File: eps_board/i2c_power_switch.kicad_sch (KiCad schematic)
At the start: 6 parts, among them U25 MCP23008T-E/SS

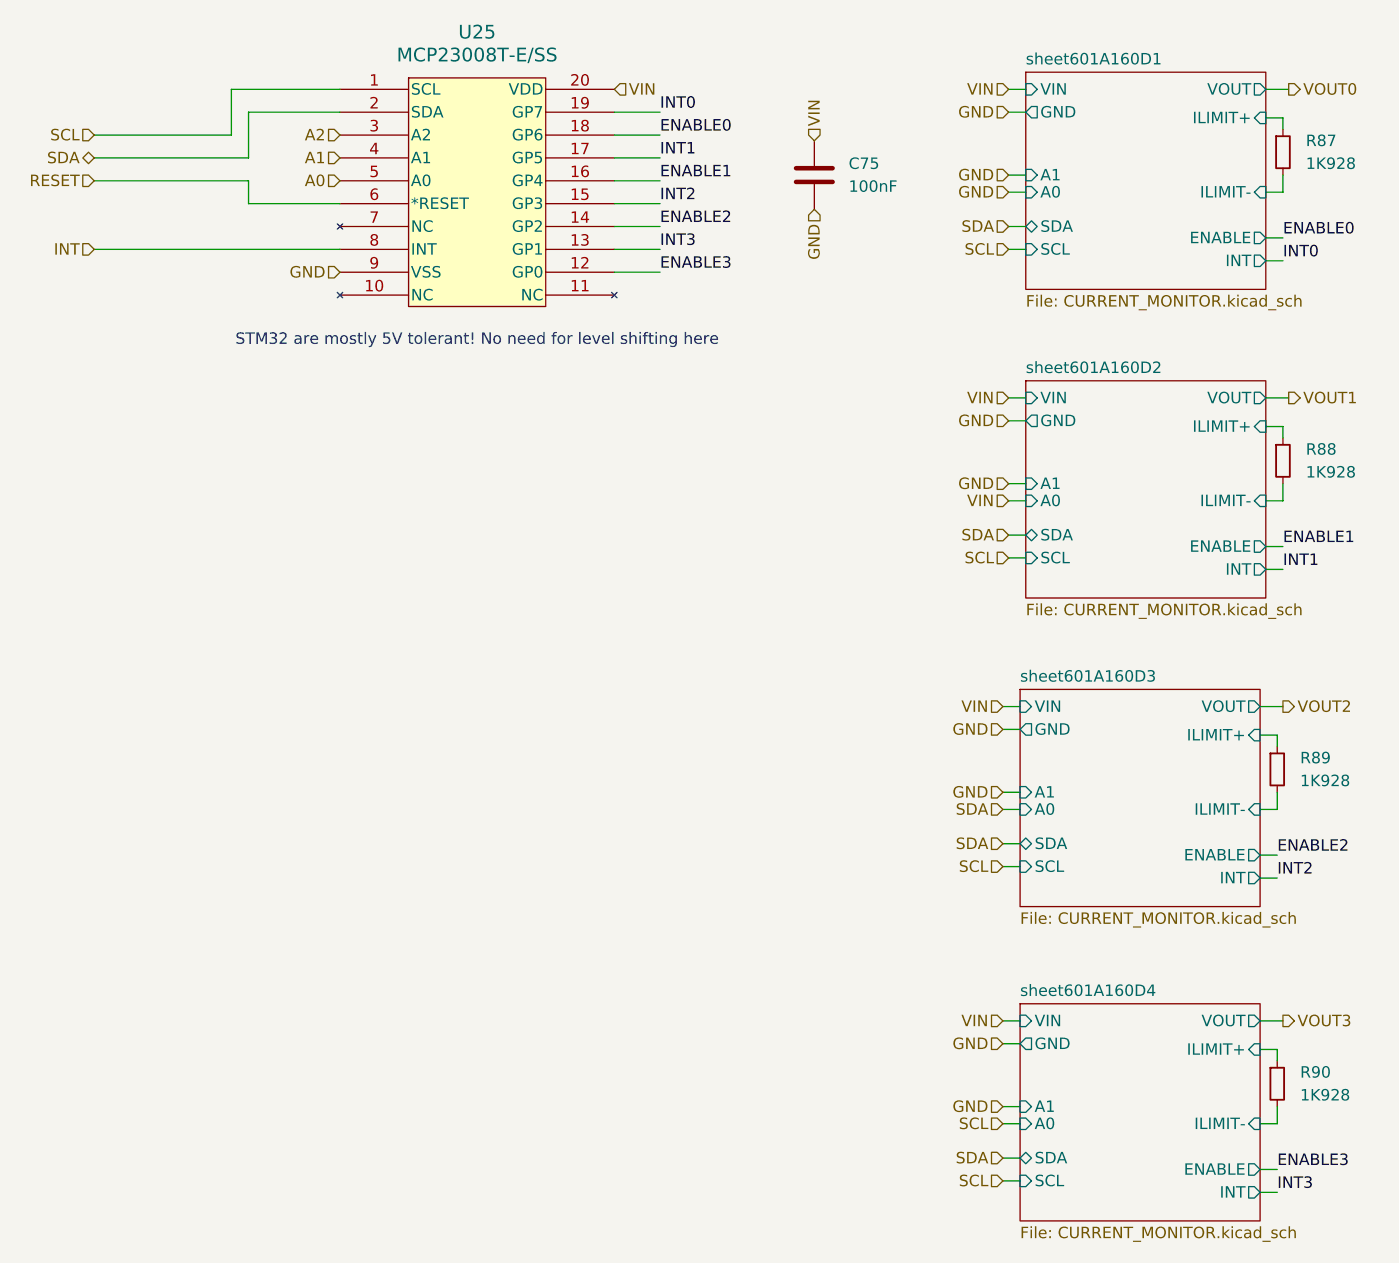
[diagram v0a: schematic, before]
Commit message: cleaning up bom: remove main camera port since it has not pullups and capacitors, correcting some errors in camera switch
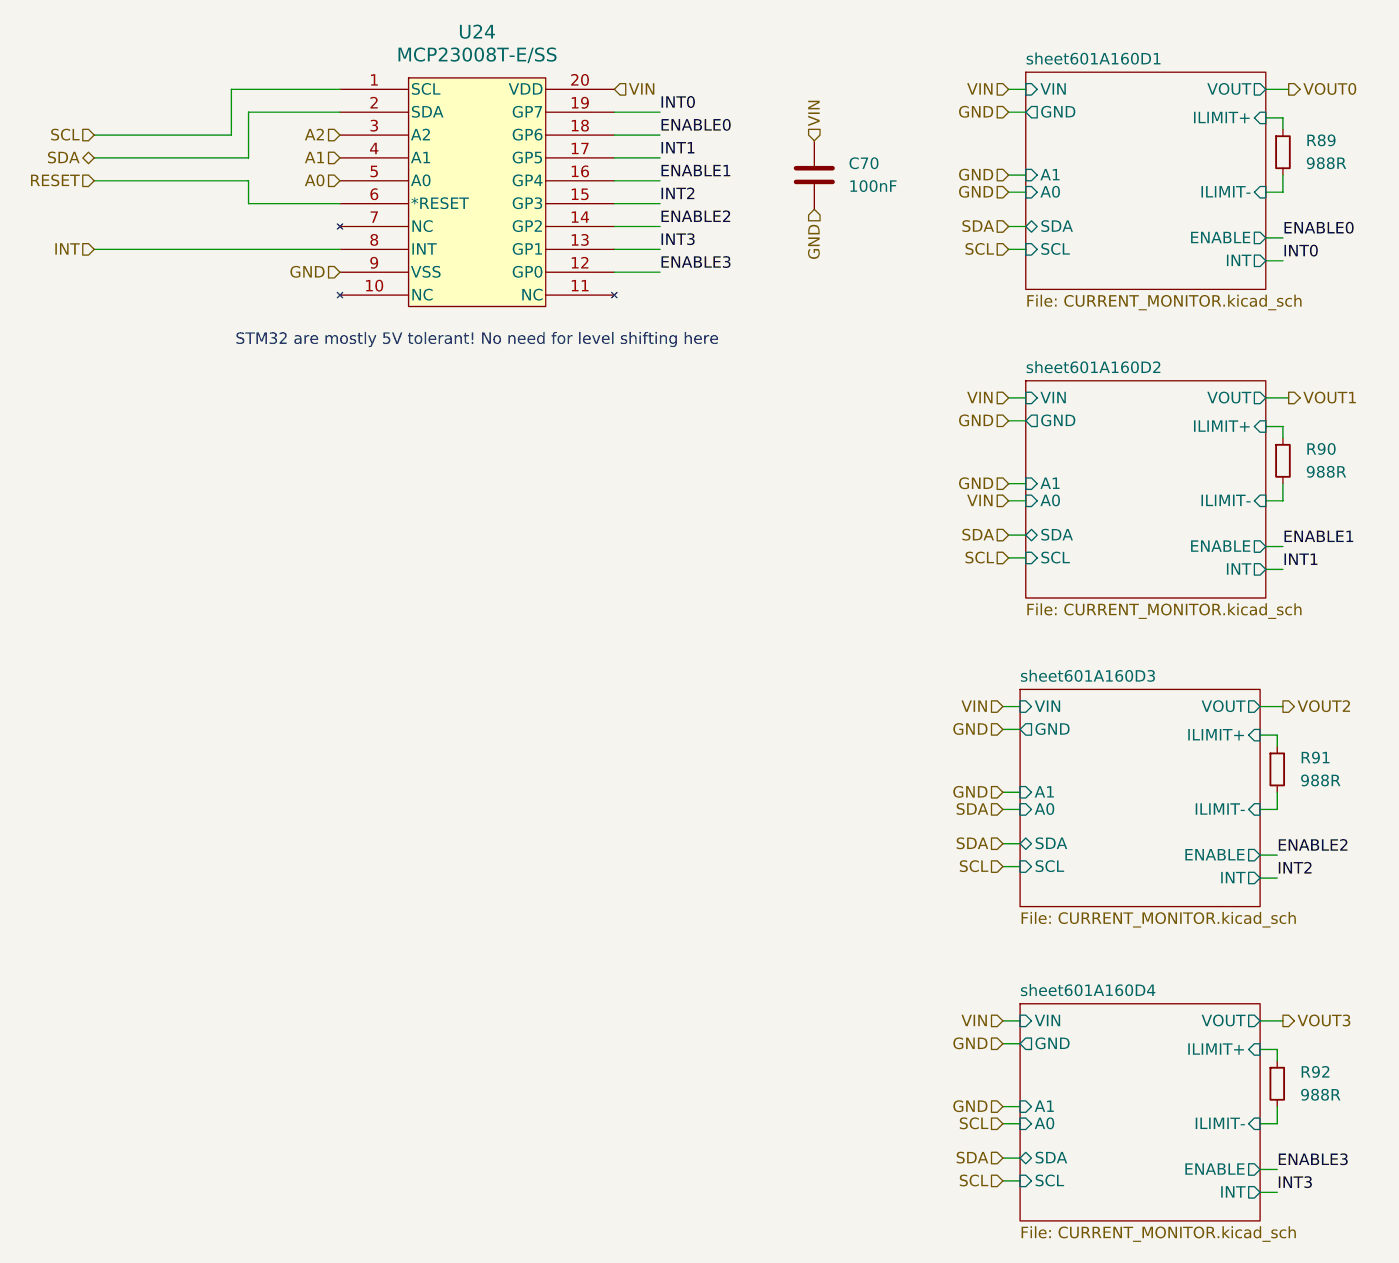
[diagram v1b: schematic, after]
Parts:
- R89: renamed from R87; value 1K928 -> 988R; Part Number RC0603FR-071K928L -> RT0603DRE07988RL; Tolerance 1 -> 0.5
- R90: renamed from R88; value 1K928 -> 988R; Part Number RC0603FR-071K928L -> RT0603DRE07988RL; Tolerance 1 -> 0.5
- R91: renamed from R89; value 1K928 -> 988R; Part Number RC0603FR-071K928L -> RT0603DRE07988RL; Tolerance 1 -> 0.5
- R92: renamed from R90; value 1K928 -> 988R; Part Number RC0603FR-071K928L -> RT0603DRE07988RL; Tolerance 1 -> 0.5
- renumbered C75 to C70, U25 to U24

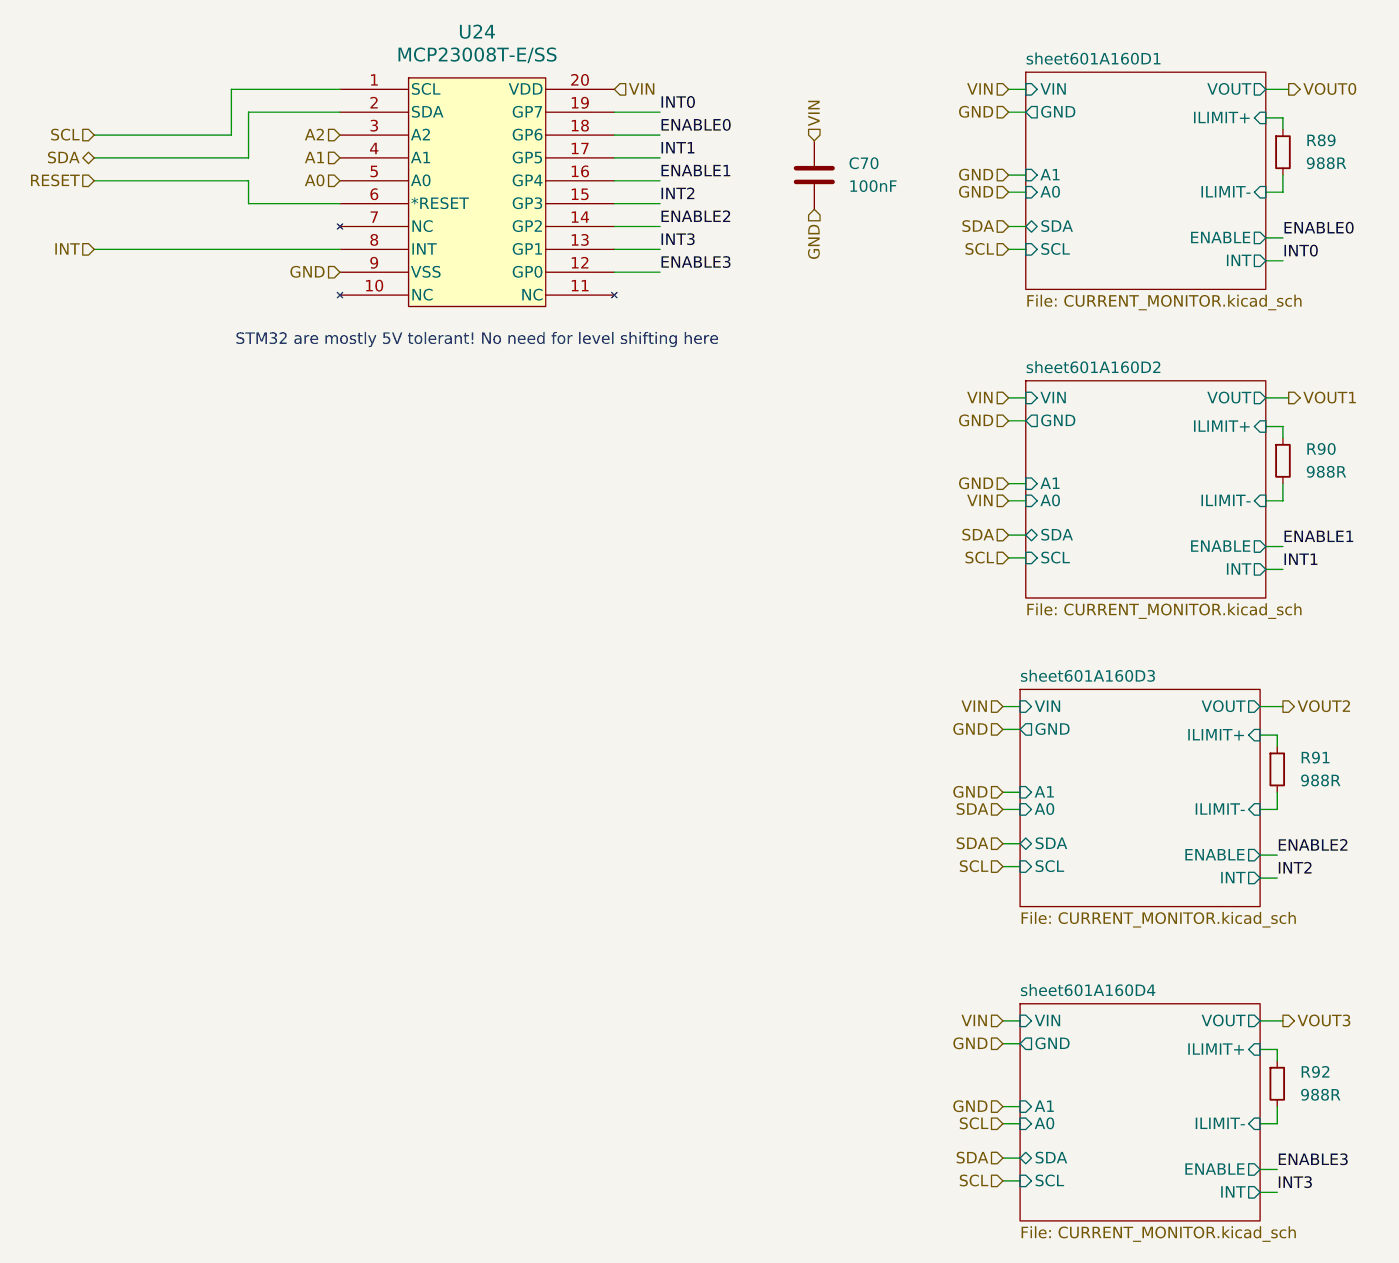
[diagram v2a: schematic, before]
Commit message: local switches and monitors for SCI and RF
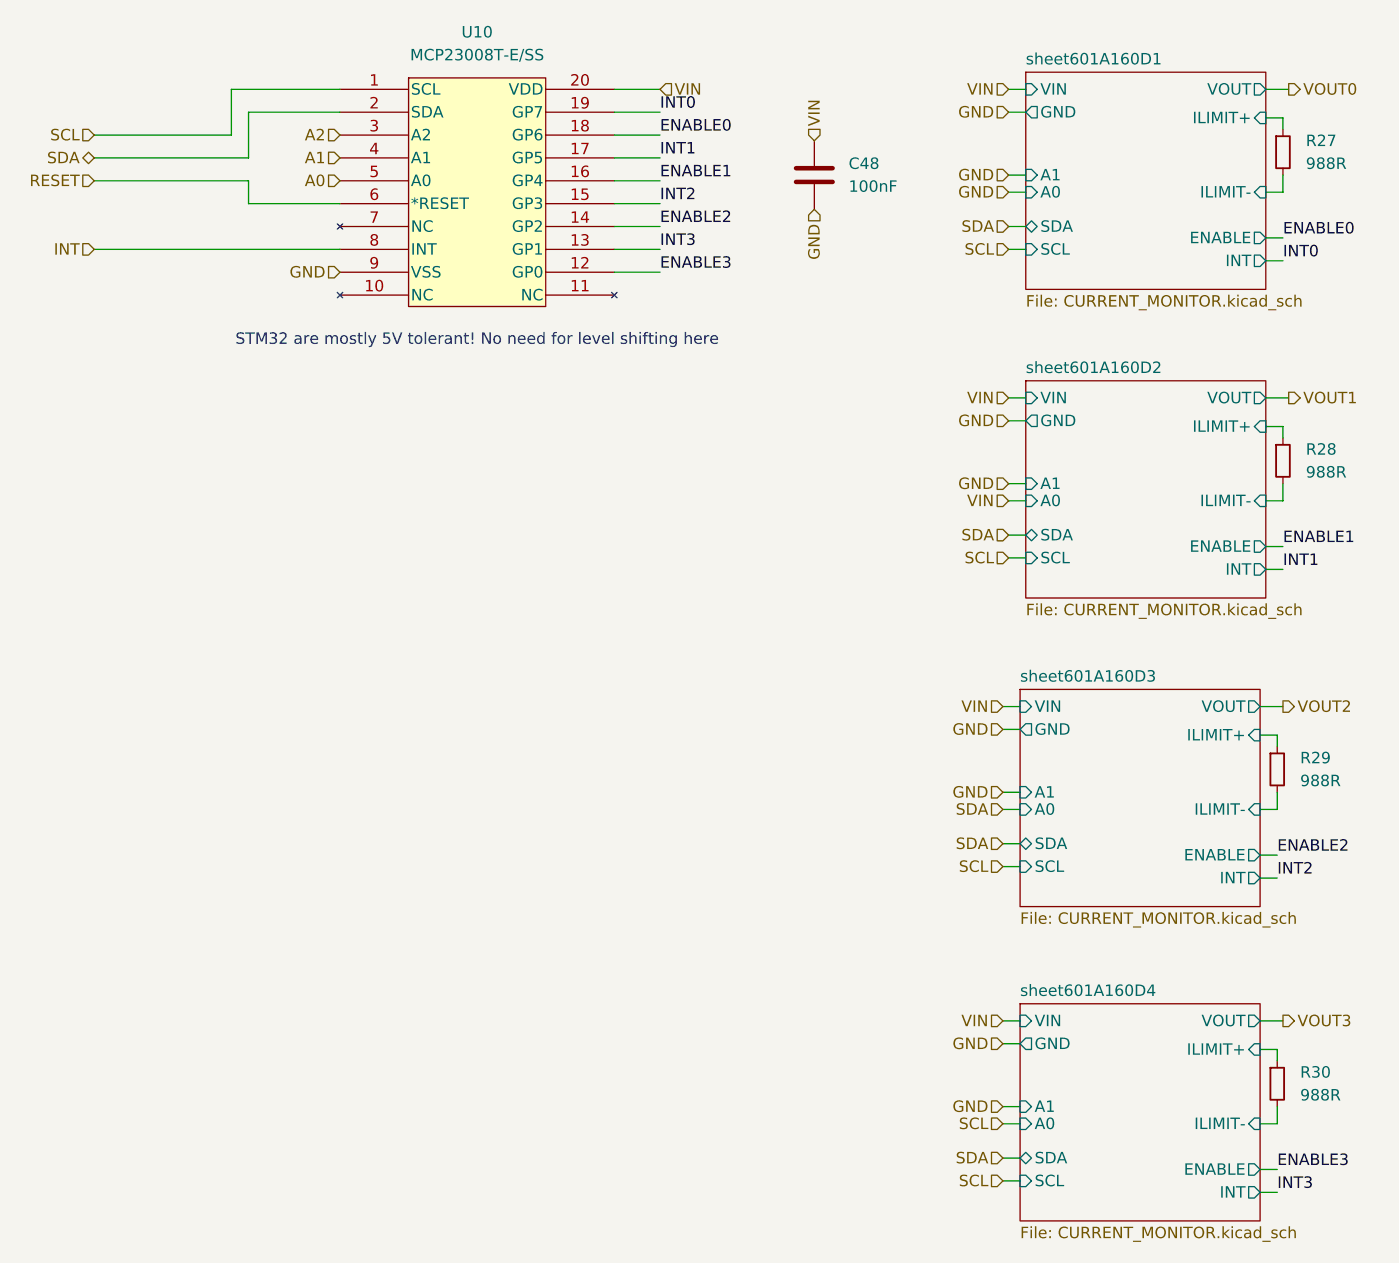
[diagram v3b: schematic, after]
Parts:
- renumbered C70 to C48, R89 to R27, R90 to R28, R91 to R29, R92 to R30, U24 to U10
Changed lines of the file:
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@@
+	(wire
+		(pts
+			(xy 100.33 31.75) (xy 95.25 31.75)
+		)
+		(stroke
+			(width 0)
+			(type default)
+		)
+	)
 	(wire
 		(pts
@@
 	(hierarchical_label "VIN"
 		(shape input)
-		(at 95.25 31.75 0)
+		(at 100.33 31.75 0)
 		(fields_autoplaced yes)
 		(effects
@@
 		(dnp no)
 		(fields_autoplaced yes)
-		(property "Reference" "C70"
+		(property "Reference" "C48"
 			(at 121.285 40.0049 0)
 			(effects
@@
 		)
 		(instances
-			(project ""
-				(path "/05170af6-30ef-4c3a-b972-f098085da1bc/53211e67-c677-4be8-893d-9825fa308902"
-					(reference "C70")
+			(project "openlst-hw"
+				(path "/a863a5ec-a5d4-4f54-be53-e8c01d5e3ac4/53f12969-e593-459a-9671-cc23a5a9aea0/158b6ecf-5b25-4ecb-8b1c-83236ab855da"
+					(reference "C48")
 					(unit 1)
 				)
@@
 		(dnp no)
 		(fields_autoplaced yes)
-		(property "Reference" "R90"
+		(property "Reference" "R28"
 			(at 172.085 71.7549 0)
 			(effects
@@
 		)
 		(instances
-			(project "EPS"
-				(path "/05170af6-30ef-4c3a-b972-f098085da1bc/53211e67-c677-4be8-893d-9825fa308902"
-					(reference "R90")
+			(project "openlst-hw"
+				(path "/a863a5ec-a5d4-4f54-be53-e8c01d5e3ac4/53f12969-e593-459a-9671-cc23a5a9aea0/158b6ecf-5b25-4ecb-8b1c-83236ab855da"
+					(reference "R28")
 					(unit 1)
 				)
@@
 		(dnp no)
 		(fields_autoplaced yes)
-		(property "Reference" "R92"
+		(property "Reference" "R30"
 			(at 171.45 140.9699 0)
 			(effects
@@
 		)
 		(instances
-			(project "EPS"
-				(path "/05170af6-30ef-4c3a-b972-f098085da1bc/53211e67-c677-4be8-893d-9825fa308902"
-					(reference "R92")
+			(project "openlst-hw"
+				(path "/a863a5ec-a5d4-4f54-be53-e8c01d5e3ac4/53f12969-e593-459a-9671-cc23a5a9aea0/158b6ecf-5b25-4ecb-8b1c-83236ab855da"
+					(reference "R30")
 					(unit 1)
 				)
@@
 		(dnp no)
 		(fields_autoplaced yes)
-		(property "Reference" "R89"
+		(property "Reference" "R27"
 			(at 172.085 37.4649 0)
 			(effects
@@
 		)
 		(instances
-			(project "EPS"
-				(path "/05170af6-30ef-4c3a-b972-f098085da1bc/53211e67-c677-4be8-893d-9825fa308902"
-					(reference "R89")
+			(project "openlst-hw"
+				(path "/a863a5ec-a5d4-4f54-be53-e8c01d5e3ac4/53f12969-e593-459a-9671-cc23a5a9aea0/158b6ecf-5b25-4ecb-8b1c-83236ab855da"
+					(reference "R27")
 					(unit 1)
 				)
@@
 		(dnp no)
 		(fields_autoplaced yes)
-		(property "Reference" "R91"
+		(property "Reference" "R29"
 			(at 171.45 106.0449 0)
 			(effects
@@
 		)
 		(instances
-			(project "EPS"
-				(path "/05170af6-30ef-4c3a-b972-f098085da1bc/53211e67-c677-4be8-893d-9825fa308902"
-					(reference "R91")
+			(project "openlst-hw"
+				(path "/a863a5ec-a5d4-4f54-be53-e8c01d5e3ac4/53f12969-e593-459a-9671-cc23a5a9aea0/158b6ecf-5b25-4ecb-8b1c-83236ab855da"
+					(reference "R29")
 					(unit 1)
 				)
@@
 		(dnp no)
 		(fields_autoplaced yes)
-		(property "Reference" "U24"
+		(property "Reference" "U10"
 			(at 80.01 25.4 0)
 			(effects
 				(font
-					(size 1.524 1.524)
+					(size 1.27 1.27)
 				)
 			)
@@
 			(effects
 				(font
-					(size 1.524 1.524)
+					(size 1.27 1.27)
 				)
 			)
@@
 		)
 		(instances
-			(project ""
-				(path "/05170af6-30ef-4c3a-b972-f098085da1bc/53211e67-c677-4be8-893d-9825fa308902"
-					(reference "U24")
+			(project "openlst-hw"
+				(path "/a863a5ec-a5d4-4f54-be53-e8c01d5e3ac4/53f12969-e593-459a-9671-cc23a5a9aea0/158b6ecf-5b25-4ecb-8b1c-83236ab855da"
+					(reference "U10")
 					(unit 1)
 				)
@@
 		)
 		(instances
-			(project "EPS"
-				(path "/05170af6-30ef-4c3a-b972-f098085da1bc/53211e67-c677-4be8-893d-9825fa308902"
-					(page "49")
+			(project "openlst-hw"
+				(path "/a863a5ec-a5d4-4f54-be53-e8c01d5e3ac4/53f12969-e593-459a-9671-cc23a5a9aea0/158b6ecf-5b25-4ecb-8b1c-83236ab855da"
+					(page "10")
 				)
 			)
@@
 		)
 		(instances
-			(project "EPS"
-				(path "/05170af6-30ef-4c3a-b972-f098085da1bc/53211e67-c677-4be8-893d-9825fa308902"
-					(page "48")
+			(project "openlst-hw"
+				(path "/a863a5ec-a5d4-4f54-be53-e8c01d5e3ac4/53f12969-e593-459a-9671-cc23a5a9aea0/158b6ecf-5b25-4ecb-8b1c-83236ab855da"
+					(page "12")
 				)
 			)
@@
 		)
 		(instances
-			(project "EPS"
-				(path "/05170af6-30ef-4c3a-b972-f098085da1bc/53211e67-c677-4be8-893d-9825fa308902"
-					(page "50")
+			(project "openlst-hw"
+				(path "/a863a5ec-a5d4-4f54-be53-e8c01d5e3ac4/53f12969-e593-459a-9671-cc23a5a9aea0/158b6ecf-5b25-4ecb-8b1c-83236ab855da"
+					(page "17")
 				)
 			)
@@
 		)
 		(instances
-			(project "EPS"
-				(path "/05170af6-30ef-4c3a-b972-f098085da1bc/53211e67-c677-4be8-893d-9825fa308902"
-					(page "51")
-				)
-			)
+			(project "openlst-hw"
+				(path "/a863a5ec-a5d4-4f54-be53-e8c01d5e3ac4/53f12969-e593-459a-9671-cc23a5a9aea0/158b6ecf-5b25-4ecb-8b1c-83236ab855da"
+					(page "9")
+				)
+			)
